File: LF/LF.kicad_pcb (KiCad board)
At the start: 2 copper layers, 105 x 58 mm, 2 parts, among them J1 SpeakON_NL4, J2 SpeakON_NL4

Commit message: changes from Trello
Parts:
- added C1: 22uF, RES:cps22, F.Cu at (92.5, 34.7)
- added G***: LOGO, PassiveFilters:fp02, F.Cu at (72.4, 28.0)
- added G***: LOGO, PassiveFilters:stakx_small_fp, B.Cu at (62.7, 70.7)
- added J3: Conn_01x02_Female, RES:Faston_DUAL_01x02_P5.08mm_D5.08mm, B.Cu at (47.9, 28.2)
- added L1: 890uH, RES:inductor_D40mm, F.Cu at (58.7, 34.7)
- added L2: 250uH, RES:inductor_P28mm, F.Cu at (72.1, 28.2)
- added R1: 100m, RES:ptc_7.2mm_larger, F.Cu at (23.4, 36.2)
- added R2: 100mΩ, RES:ptc_7.2mm_larger, F.Cu at (27.3, 36.2)
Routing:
- added copper zone on F.Cu, net Net-(C1-Pad1)
- added copper zone on F.Cu, net Net-(J3-Pad1)
- added copper zone on B.Cu, net Net-(L1-Pad2)
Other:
- outline, holes or cut-outs redrawn
- board text added: "+"
- board text added: "-"
- board text added: "1+"
- board text added: "1-"
- board text added: "2+"
- board text added: "890uH"
- board text added: "JLCJLCJLCJLC"
- board text added: "MINISOUND LF"

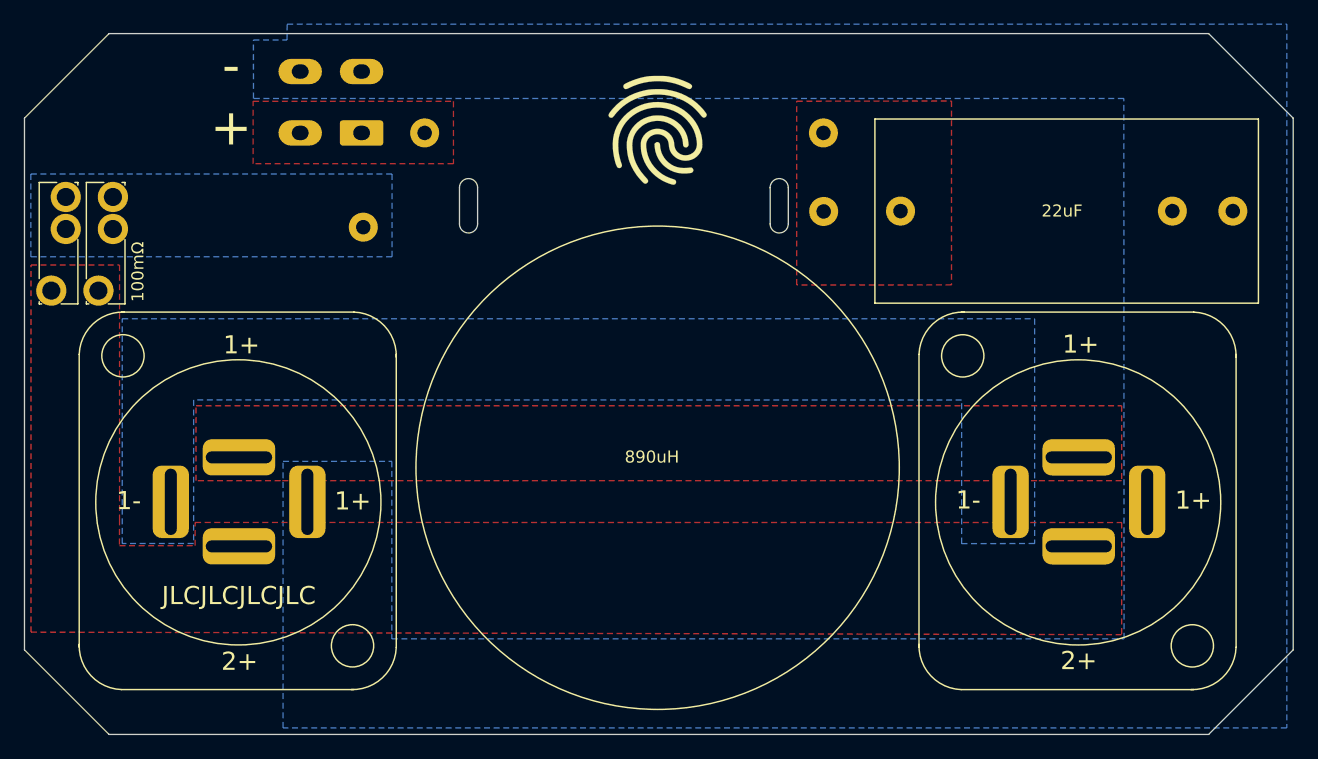
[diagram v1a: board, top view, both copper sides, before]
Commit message: added parallel board
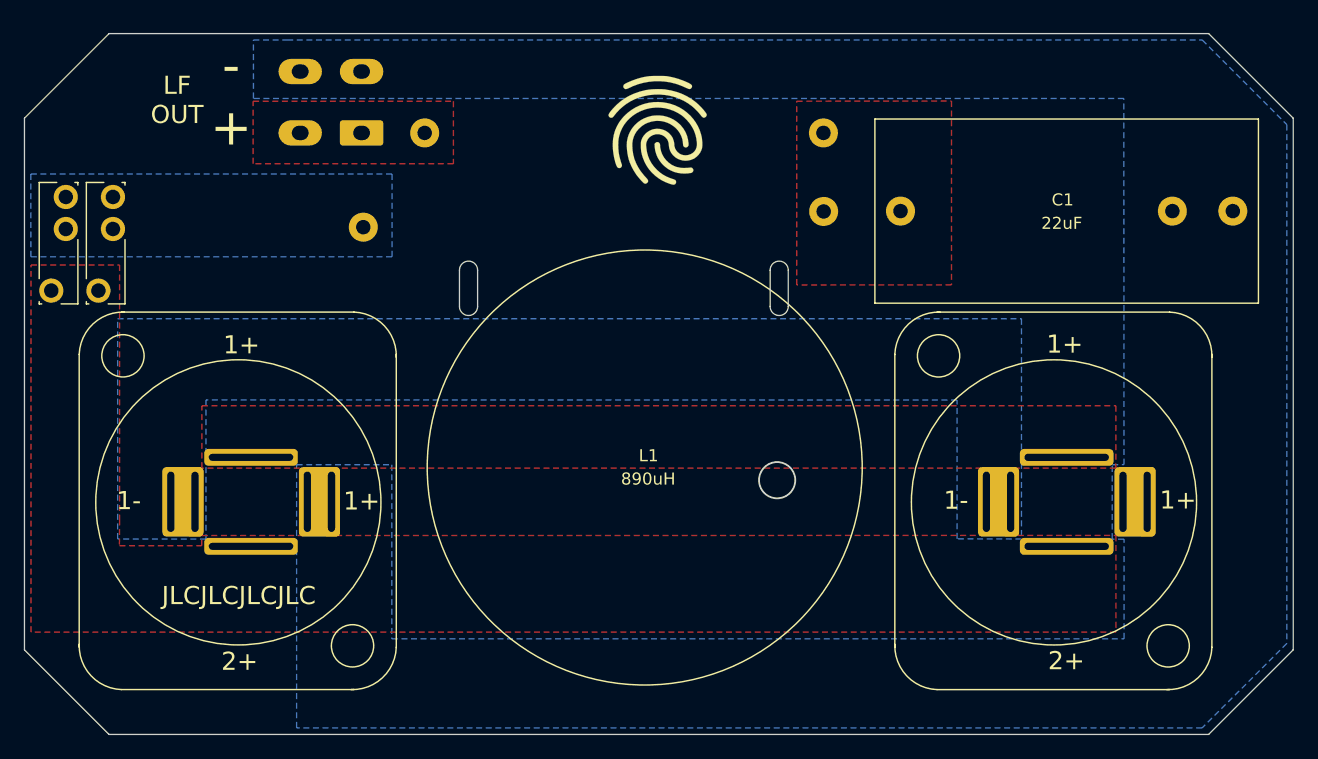
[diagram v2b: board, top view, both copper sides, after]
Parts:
- J1, J2: footprint SpeakON:NL4MP-M3 -> SpeakON:NL4MP-M3_double_left
- moved J2 2.00 mm to (105.2, 55.1)
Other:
- outline, holes or cut-outs redrawn
- board text added: "240uH"
- board text added: "L2"
- board text added: "LF OUT"
- board text removed: "890uH"
